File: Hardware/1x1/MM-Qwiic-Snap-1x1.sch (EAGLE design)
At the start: 49 parts, among them J15 MICROMOD-2222-C, J2 QWIIC_RIGHT_ANGLE, U1 MCP73831, U5 AP7361C-33FGEUDFN-8

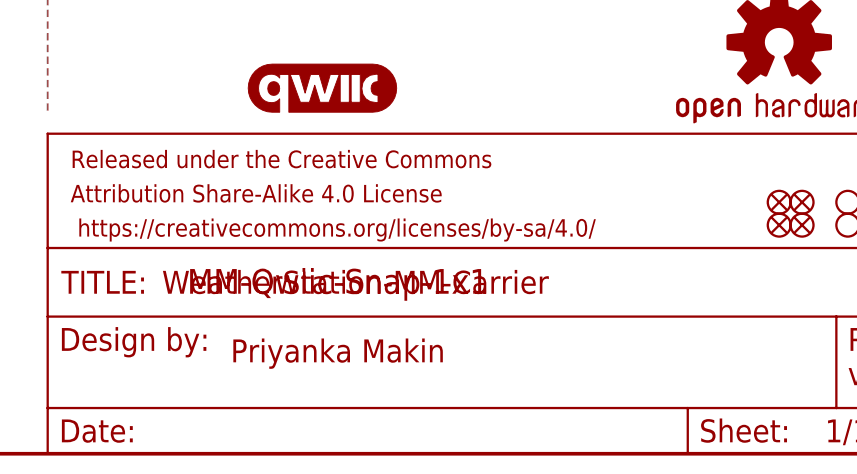
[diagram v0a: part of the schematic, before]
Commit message: Create 2x1 version and generate production files
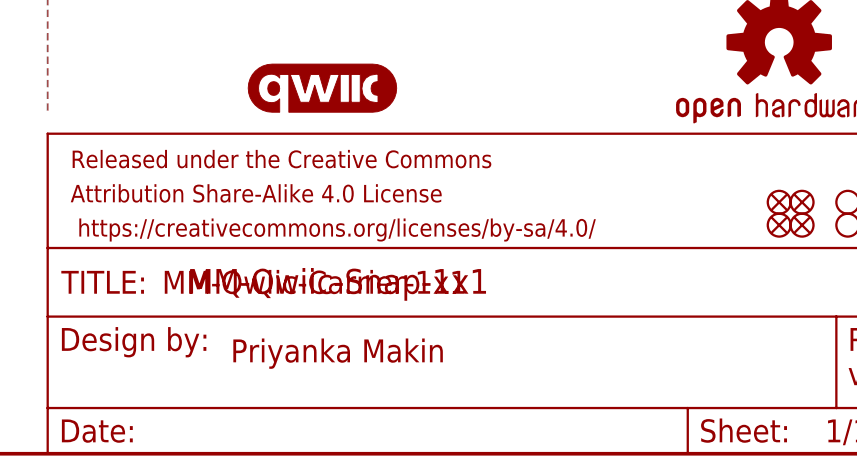
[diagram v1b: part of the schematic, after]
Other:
- note added: "MM-Qwiic-Carrier-1x1"
- note removed: "WeatherStation-MM-Carrier"
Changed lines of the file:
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@@
 <?xml version="1.0" encoding="utf-8"?>
 <!DOCTYPE eagle SYSTEM "eagle.dtd">
-<eagle version="9.5.2">
+<eagle version="9.6.2">
 <drawing>
 <settings>
@@
 <text x="58.674" y="263.906" size="2.54" layer="94" font="vector" align="center">Universal MicroMod Connector</text>
 <text x="350.52" y="10.16" size="2.54" layer="94" font="vector">Priyanka Makin</text>
-<text x="342.9" y="17.78" size="2.54" layer="94" font="vector">WeatherStation-MM-Carrier</text>
+<text x="342.9" y="17.78" size="2.54" layer="94" font="vector">MM-Qwiic-Carrier-1x1</text>
 <text x="142.24" y="238.76" size="2.54" layer="94" font="vector" align="center">LED</text>
 <text x="419.1" y="7.62" size="2.54" layer="94" font="vector">v01</text>
